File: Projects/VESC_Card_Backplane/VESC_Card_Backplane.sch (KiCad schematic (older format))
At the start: 0 parts

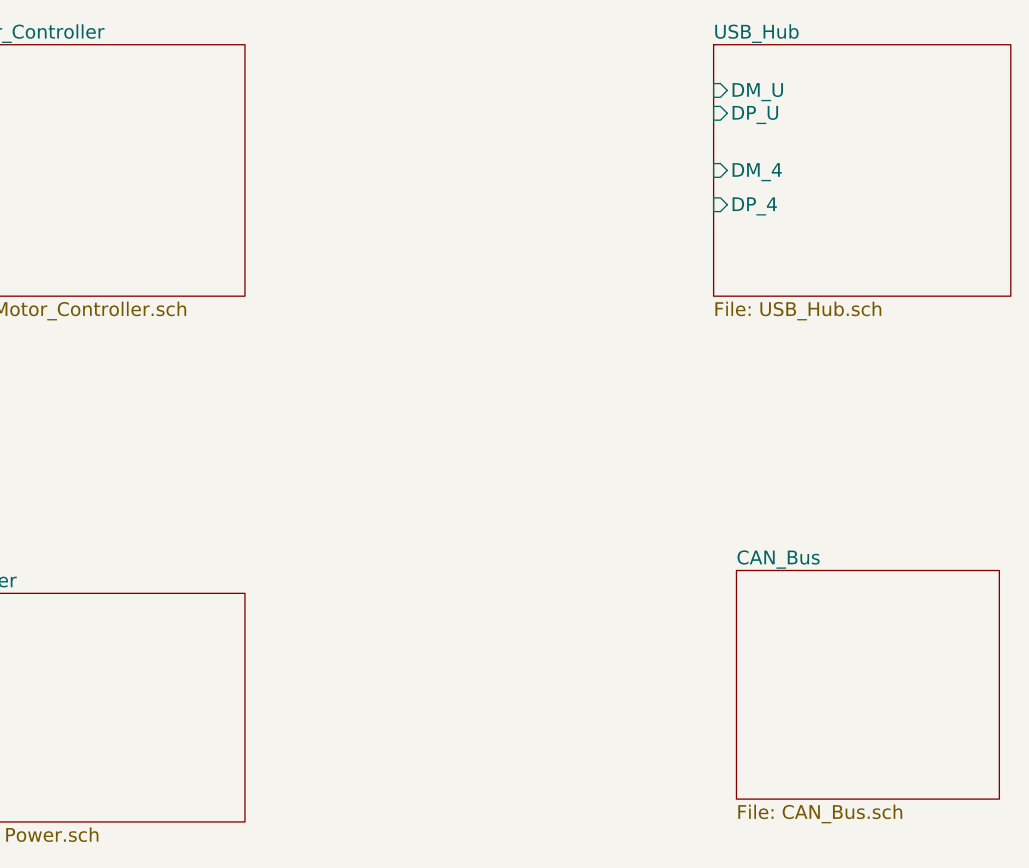
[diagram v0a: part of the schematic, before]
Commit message: Added stuff to VESC_Card_Backplane
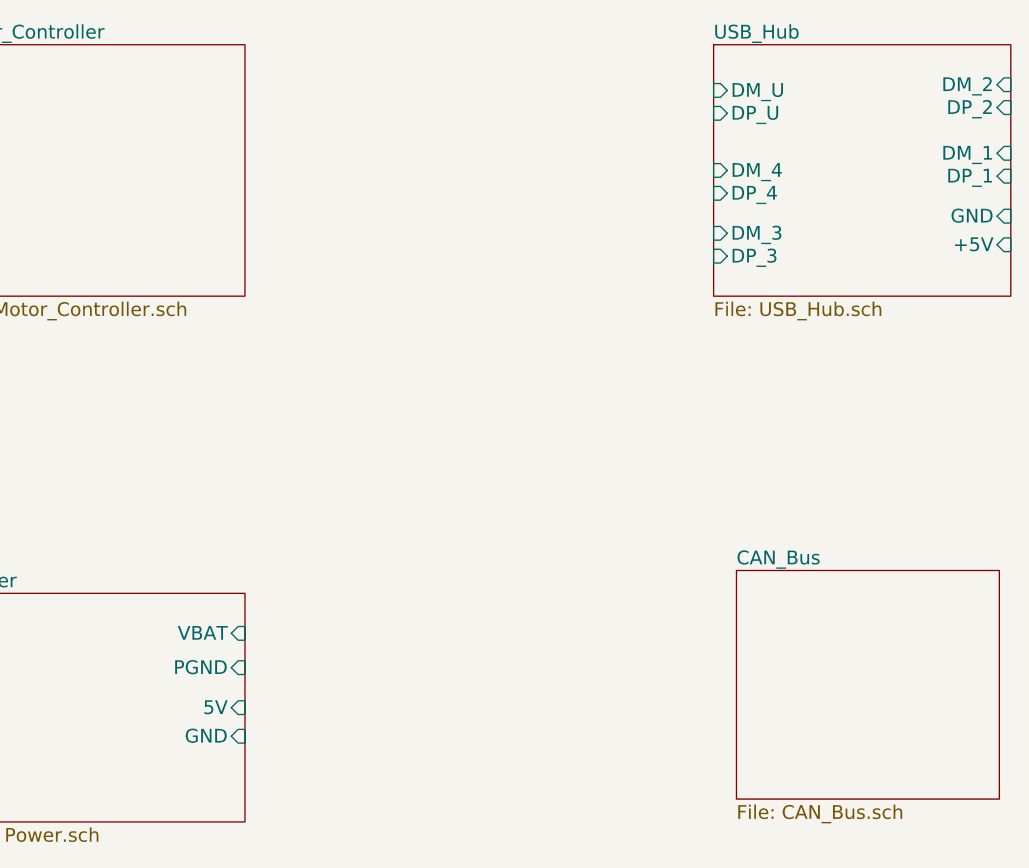
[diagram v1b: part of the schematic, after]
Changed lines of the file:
@@
 F3 "DP_U" I L 7050 2250 60
 F4 "DM_4" I L 7050 2500 60
-F5 "DP_4" I L 7050 2650 60
+F5 "DP_4" I L 7050 2600 60
+F6 "DM_3" I L 7050 2775 60
+F7 "DP_3" I L 7050 2875 60
+F8 "DM_2" I R 8350 2125 60
+F9 "DP_2" I R 8350 2225 60
+F10 "DM_1" I R 8350 2425 60
+F11 "DP_1" I R 8350 2525 60
+F12 "GND" I R 8350 2700 60
+F13 "+5V" I R 8350 2825 60
 $EndSheet
 $Sheet
@@
 F0 "Power" 60
 F1 "Power.sch" 60
+F2 "VBAT" I R 5000 4525 60
+F3 "PGND" I R 5000 4675 60
+F4 "5V" I R 5000 4850 60
+F5 "GND" I R 5000 4975 60
 $EndSheet
 $Sheet

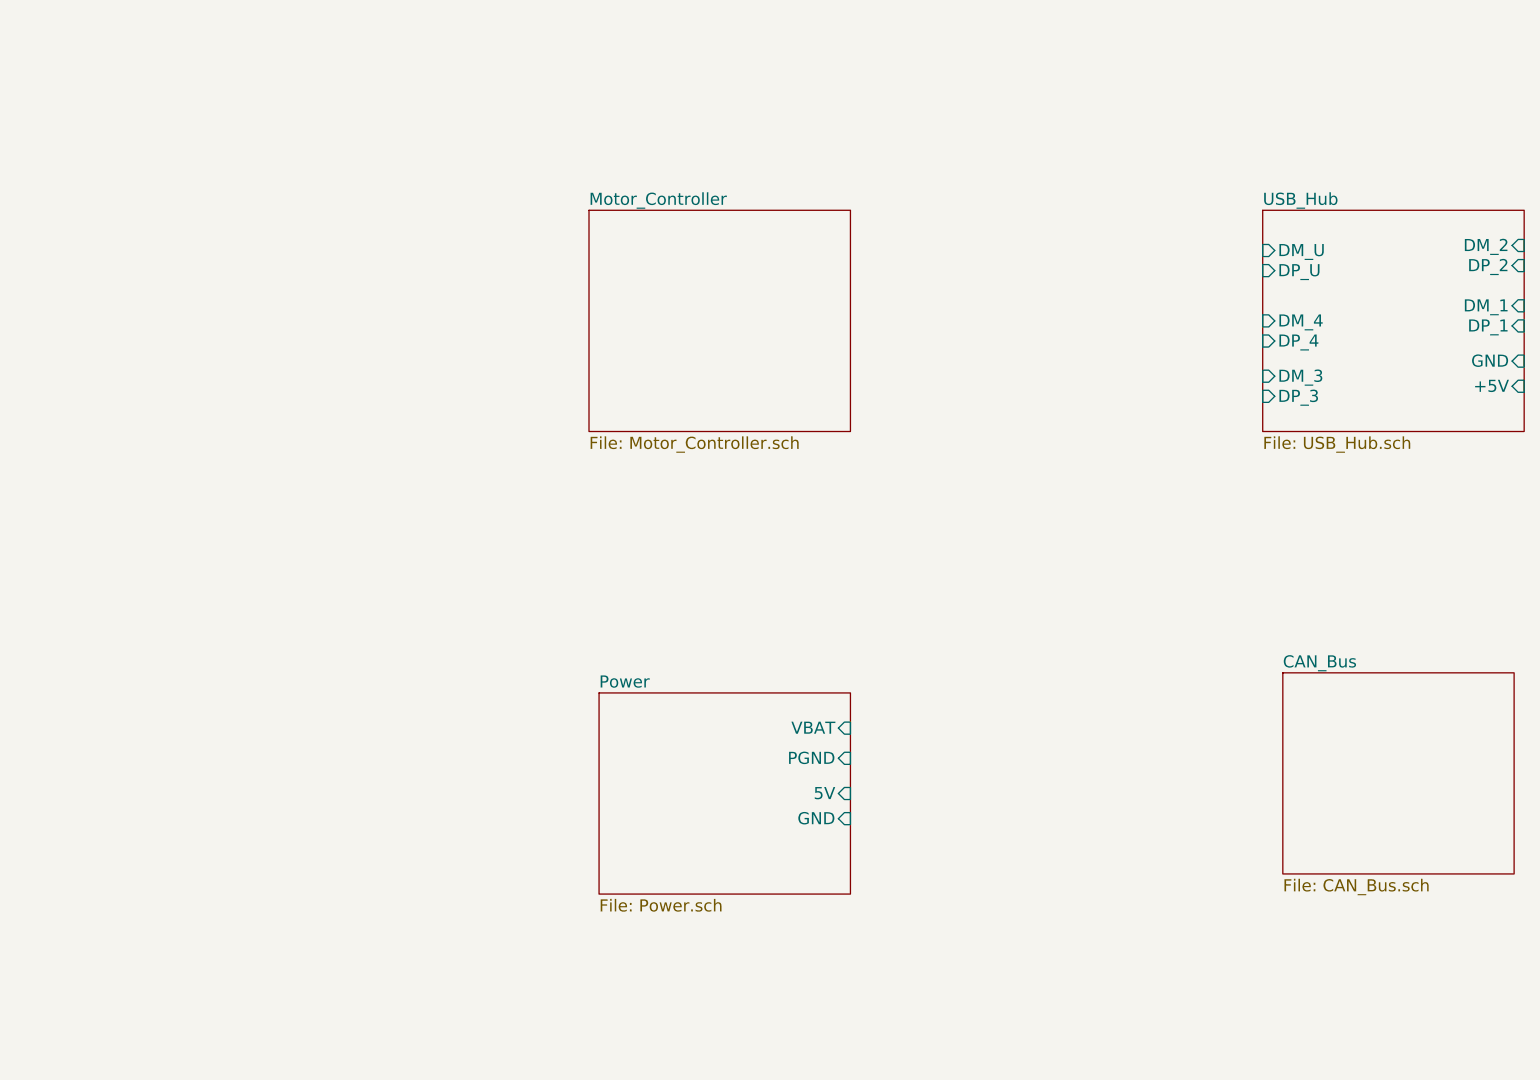
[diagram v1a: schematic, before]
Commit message: Updated subsheets and added CAN bus :)
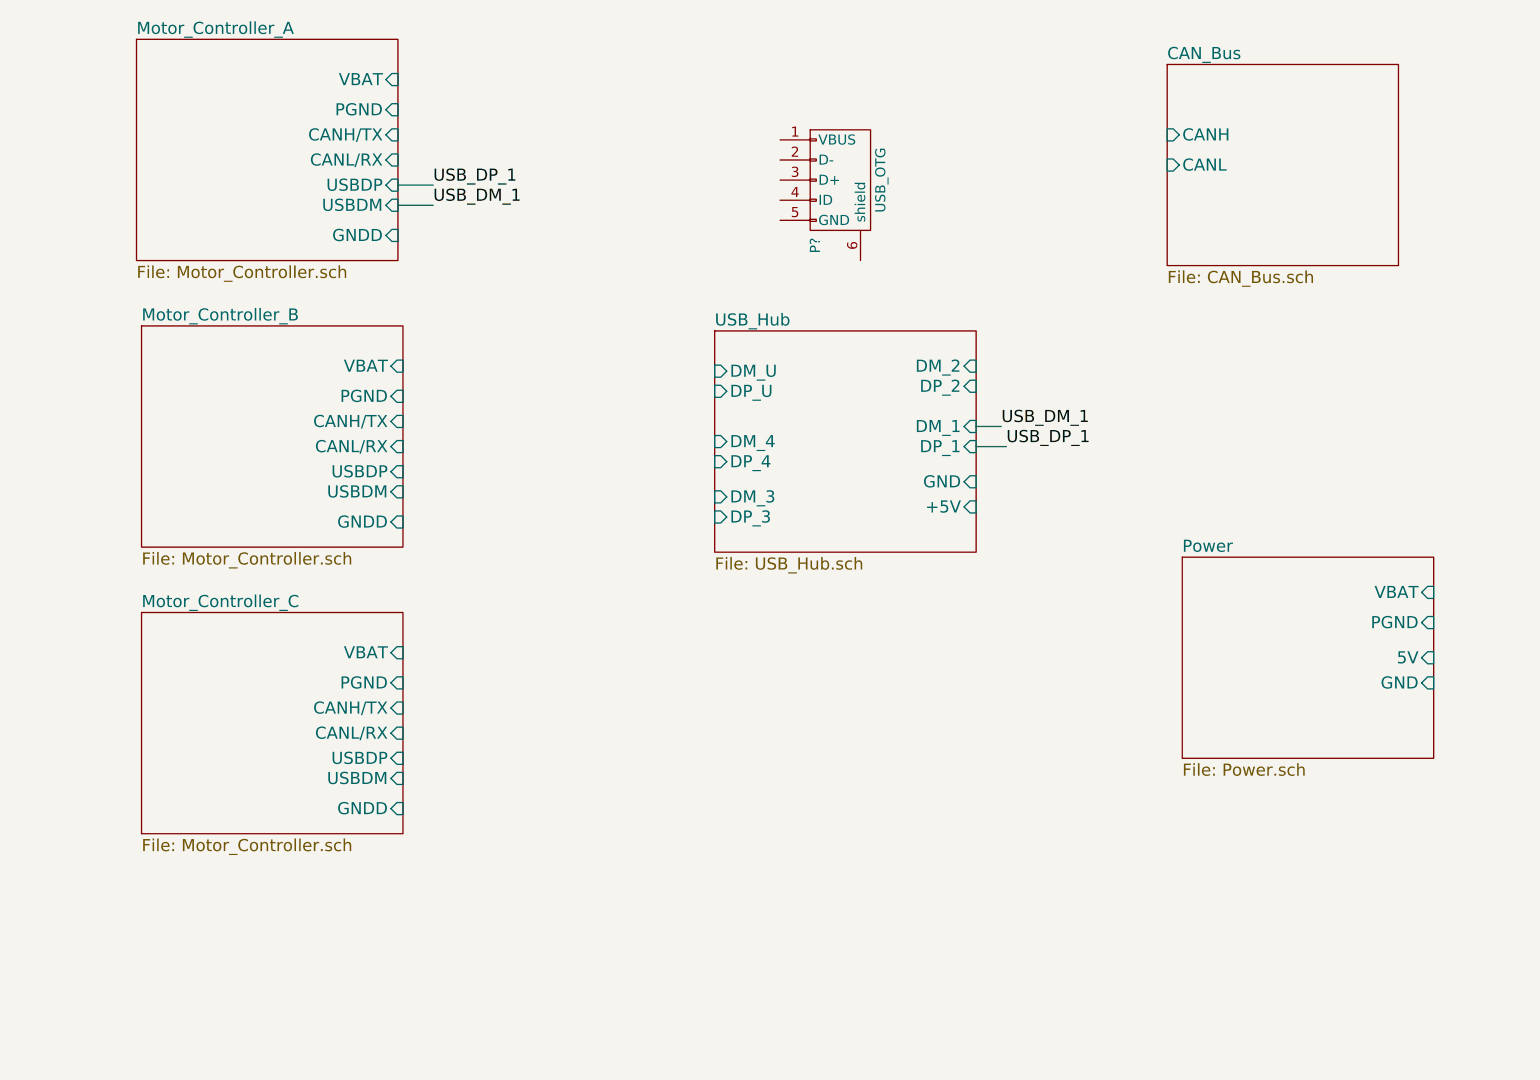
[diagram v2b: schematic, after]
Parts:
- added P?: USB_OTG, symbol USB_OTG
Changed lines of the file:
@@
 $Descr A4 11693 8268
 encoding utf-8
-Sheet 1 5
+Sheet 1 6
 Title ""
 Date ""
@@
 $EndDescr
 $Sheet
-S 7050 1950 1300 1100
+S 4325 2550 1300 1100
 U 5871A1CF
 F0 "USB_Hub" 60
 F1 "USB_Hub.sch" 60
-F2 "DM_U" I L 7050 2150 60
-F3 "DP_U" I L 7050 2250 60
-F4 "DM_4" I L 7050 2500 60
-F5 "DP_4" I L 7050 2600 60
-F6 "DM_3" I L 7050 2775 60
-F7 "DP_3" I L 7050 2875 60
-F8 "DM_2" I R 8350 2125 60
-F9 "DP_2" I R 8350 2225 60
-F10 "DM_1" I R 8350 2425 60
-F11 "DP_1" I R 8350 2525 60
-F12 "GND" I R 8350 2700 60
-F13 "+5V" I R 8350 2825 60
+F2 "DM_U" I L 4325 2750 60
+F3 "DP_U" I L 4325 2850 60
+F4 "DM_4" I L 4325 3100 60
+F5 "DP_4" I L 4325 3200 60
+F6 "DM_3" I L 4325 3375 60
+F7 "DP_3" I L 4325 3475 60
+F8 "DM_2" I R 5625 2725 60
+F9 "DP_2" I R 5625 2825 60
+F10 "DM_1" I R 5625 3025 60
+F11 "DP_1" I R 5625 3125 60
+F12 "GND" I R 5625 3300 60
+F13 "+5V" I R 5625 3425 60
 $EndSheet
 $Sheet
-S 3700 1950 1300 1100
+S 1450 1100 1300 1100
 U 5871DA4F
-F0 "Motor_Controller" 60
+F0 "Motor_Controller_A" 60
 F1 "Motor_Controller.sch" 60
+F2 "VBAT" I R 2750 1300 60
+F3 "PGND" I R 2750 1450 60
+F4 "CANH/TX" I R 2750 1575 60
+F5 "CANL/RX" I R 2750 1700 60
+F6 "USBDP" I R 2750 1825 60
+F7 "USBDM" I R 2750 1925 60
+F8 "GNDD" I R 2750 2075 60
 $EndSheet
 $Sheet
-S 3750 4350 1250 1000
+S 6650 3675 1250 1000
 U 5871DB4E
 F0 "Power" 60
 F1 "Power.sch" 60
-F2 "VBAT" I R 5000 4525 60
-F3 "PGND" I R 5000 4675 60
-F4 "5V" I R 5000 4850 60
-F5 "GND" I R 5000 4975 60
+F2 "VBAT" I R 7900 3850 60
+F3 "PGND" I R 7900 4000 60
+F4 "5V" I R 7900 4175 60
+F5 "GND" I R 7900 4300 60
 $EndSheet
 $Sheet
-S 7150 4250 1150 1000
+S 6575 1225 1150 1000
 U 5871E13C
 F0 "CAN_Bus" 60
 F1 "CAN_Bus.sch" 60
+F2 "CANH" I L 6575 1575 60
+F3 "CANL" I L 6575 1725 60
 $EndSheet
+$Sheet
+S 1475 2525 1300 1100
+U 5878CF59
+F0 "Motor_Controller_B" 60
+F1 "Motor_Controller.sch" 60
+F2 "VBAT" I R 2775 2725 60
+F3 "PGND" I R 2775 2875 60
+F4 "CANH/TX" I R 2775 3000 60
+F5 "CANL/RX" I R 2775 3125 60
+F6 "USBDP" I R 2775 3250 60
+F7 "USBDM" I R 2775 3350 60
+F8 "GNDD" I R 2775 3500 60
+$EndSheet
+$Sheet
+S 1475 3950 1300 1100
+U 5878D5C8
+F0 "Motor_Controller_C" 60
+F1 "Motor_Controller.sch" 60
+F2 "VBAT" I R 2775 4150 60
+F3 "PGND" I R 2775 4300 60
+F4 "CANH/TX" I R 2775 4425 60
+F5 "CANL/RX" I R 2775 4550 60
+F6 "USBDP" I R 2775 4675 60
+F7 "USBDM" I R 2775 4775 60
+F8 "GNDD" I R 2775 4925 60
+$EndSheet
+Wire Wire Line
+	2750 1825 2925 1825
+Wire Wire Line
+	2750 1925 2925 1925
+Text Label 2925 1825 0    60   ~ 0
+USB_DP_1
+Text Label 2925 1925 0    60   ~ 0
+USB_DM_1
+Wire Wire Line
+	5625 3125 5775 3125
+Text Label 5775 3125 0    60   ~ 0
+USB_DP_1
+Wire Wire Line
+	5625 3025 5750 3025
+Text Label 5750 3025 0    60   ~ 0
+USB_DM_1
+$Comp
+L USB_OTG P?
+U 1 1 58790821
+P 4950 1800
+F 0 "P?" H 5275 1675 50  0000 C CNN
+F 1 "USB_OTG" H 4950 2000 50  0000 C CNN
+F 2 "" V 4900 1700 50  0000 C CNN
+F 3 "" V 4900 1700 50  0000 C CNN
+	1    4950 1800
+	0    1    1    0
+$EndComp
 $EndSCHEMATC
